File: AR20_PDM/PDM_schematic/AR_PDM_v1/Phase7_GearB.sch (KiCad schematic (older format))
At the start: 15 parts, among them Q1 BTS50025-1TAD, U1 INA233

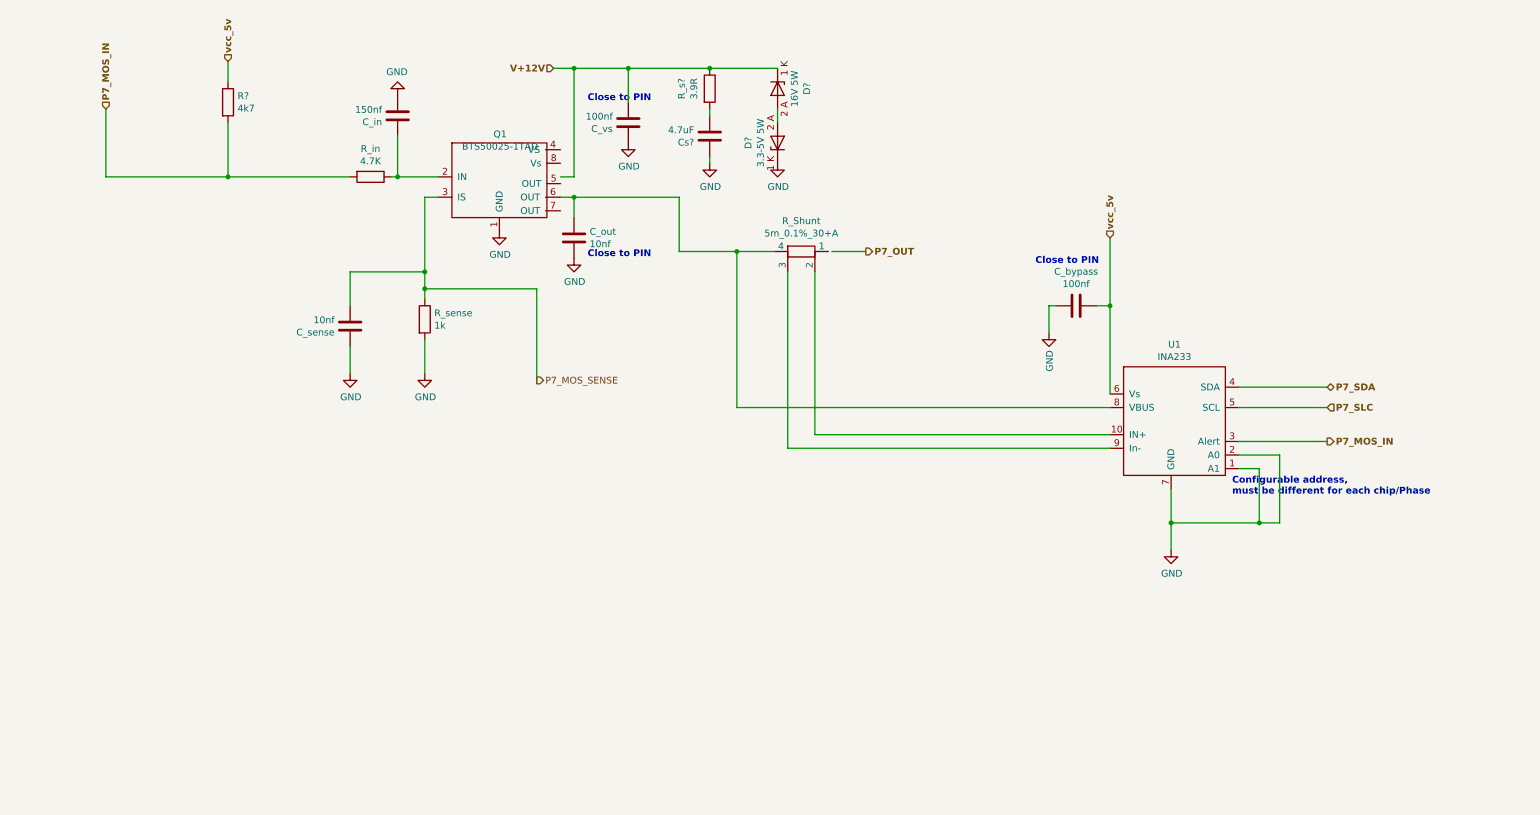
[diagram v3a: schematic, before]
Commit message: Fixed issues, controlled components, BOM, see discription
- added acm symbol
- fixed wrongly faced P-mosfets
- I/O expander now sinks led instead of source
- Bill of material mostly done
- Correct address for INA233 chips.
- Now 4 diodes serves as flyback for all mosfets
- Corrected naming scheme for compmonents (everything is not fixed yet)
- Fixed some labels
- altso some minor changes
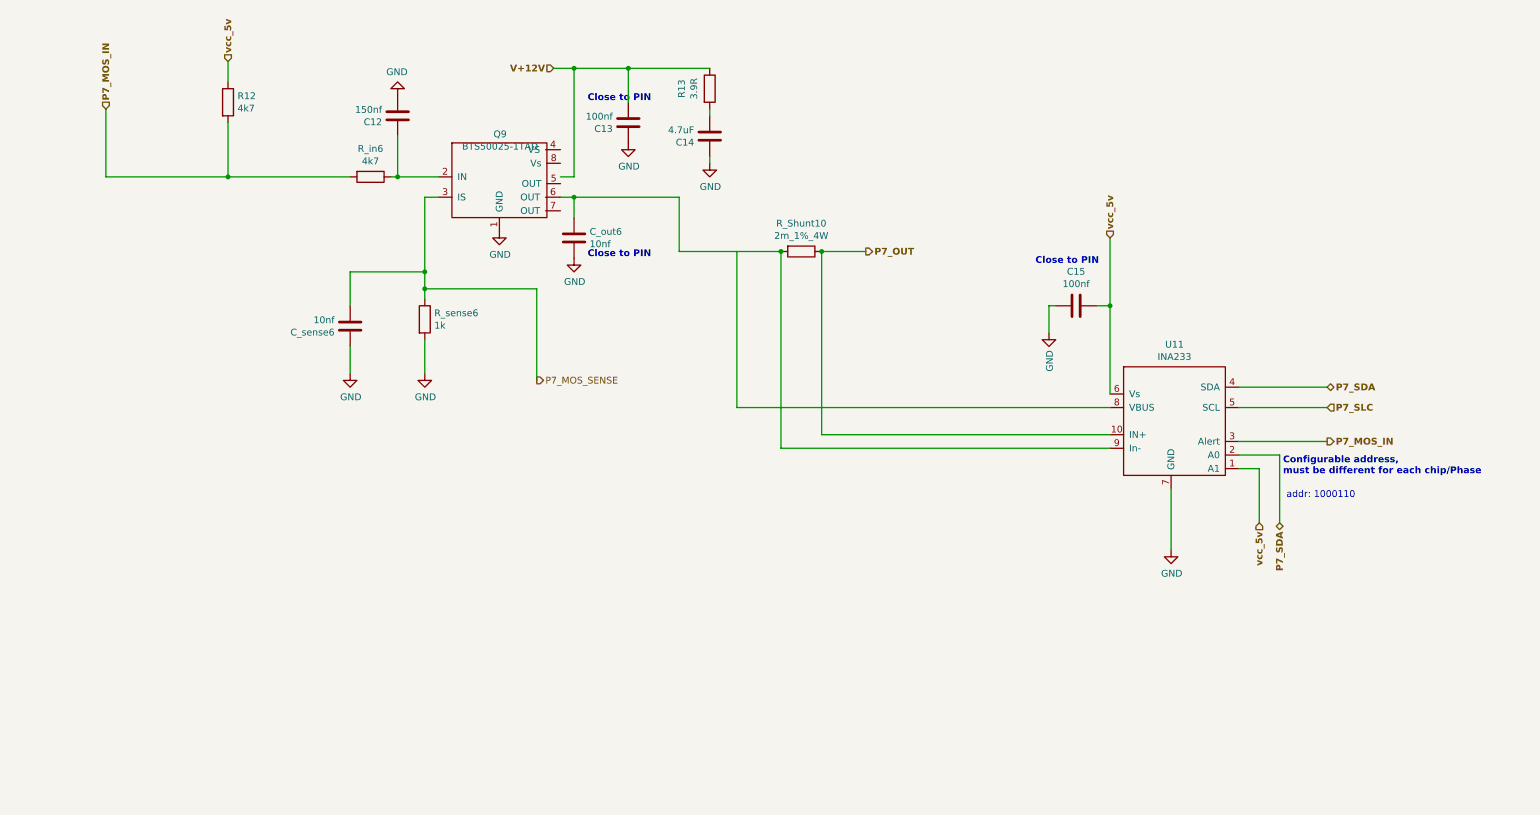
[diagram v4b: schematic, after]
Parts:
- removed C_bypass, C_vs: 100nf, symbol AR20_PDM_v1-rescue:C-Device
- removed C_in: 150nf, symbol AR20_PDM_v1-rescue:C-Device
- removed C_out, C_sense: 10nf, symbol AR20_PDM_v1-rescue:C-Device
- removed Cs?: 4.7uF, symbol AR20_PDM_v1-rescue:C-Device
- removed D?: 3.3-5V 5W, symbol AR20_PDM_v1-rescue:D_Zener-Device
- removed D?: 16V 5W, symbol AR20_PDM_v1-rescue:D_Zener-Device
- removed Q1: BTS50025-1TAD, symbol AR20_PDM_v1-rescue:BTS50025-1TAD
- removed R?: 4k7, symbol AR20_PDM_v1-rescue:R-Device
- removed R_Shunt: 5m_0.1%_30+A, symbol AR20_PDM_v1-rescue:R_Shunt-Device
- removed U1: INA233, symbol AR20_PDM_v1-rescue:INA233
- added C12: 150nf, Capacitor_SMD:C_0603_1608Metric, symbol AR20_PDM_v1-rescue:C-Device
- added C13, C15: 100nf, Capacitor_SMD:C_0603_1608Metric, symbol AR20_PDM_v1-rescue:C-Device
- added C14: 4.7uF, Capacitor_SMD:C_1206_3216Metric, symbol AR20_PDM_v1-rescue:C-Device
- added C_out6, C_sense6: 10nf, Capacitor_SMD:C_0603_1608Metric, symbol AR20_PDM_v1-rescue:C-Device
- added Q9: BTS50025-1TAD, symbol AR20_PDM_v1-rescue:BTS50025-1TAD
- added R12: 4k7, symbol AR20_PDM_v1-rescue:R-Device
- added R_Shunt10: 2m_1%_4W, symbol AR20_PDM_v1-rescue:R-Device
- added U11: INA233, symbol AR20_PDM_v1-rescue:INA233
- R_in6: renamed from R_in; value 4.7K -> 4k7
- gave numbers to parts that had none: 1
- renumbered R_sense to R_sense6
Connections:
- wire segments 57 -> 52
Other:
- note added: "addr: 1000110"

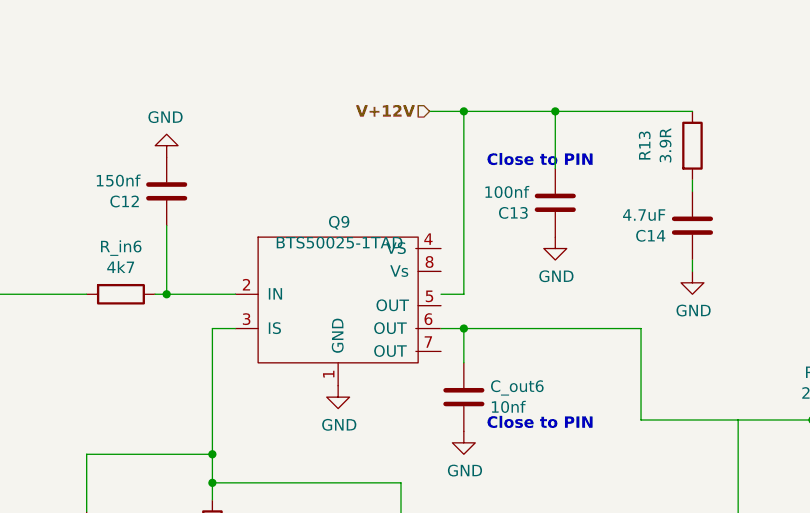
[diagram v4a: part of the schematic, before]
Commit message: PCB design, and issue fixing, work in progress
- Error fixed: Mux mosfet resistor change to ground
- Open drain output added on phase 6, for engine blipping purpose
- Most of pcb symbols and footprints are finished, including main connector
- PCB is change from 1oz to 2oz copper layer, for easier routing.
- Basic Draft of pcb is done, for now.
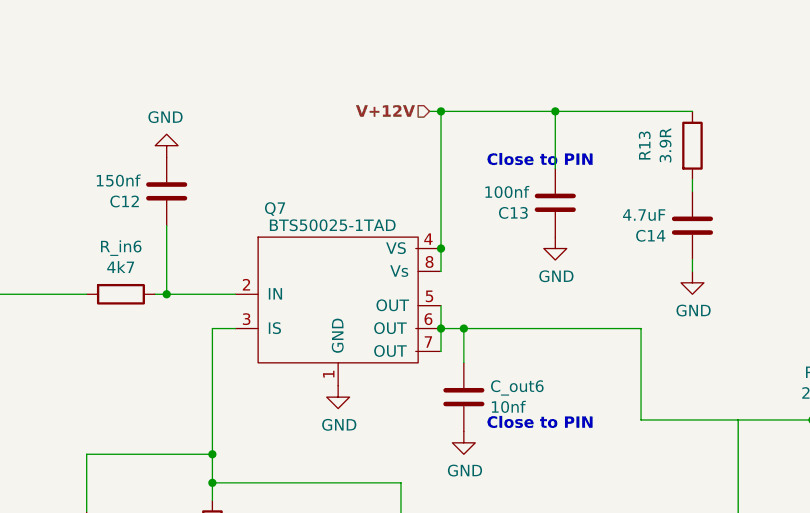
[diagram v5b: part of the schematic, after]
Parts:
- Q7: renamed from Q9; footprint (none) -> AR_PDM_v1:BTS500xx
- R12, R13, R_in6, R_sense6: footprint (none) -> Resistor_SMD:R_0603_1608Metric
- R_Shunt10: footprint (none) -> Resistor_SMD:R_2512_6332Metric
- U11: footprint (none) -> AR_PDM_v1:INA233
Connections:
- net V+12V: now also Q7.4 (VS), Q7.8 (Vs)
- net at C_out6.1, Q7.6 (OUT), R_Shunt10.2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: now also Q7.5 (OUT), Q7.7 (OUT)
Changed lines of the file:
@@
 F 0 "R_in6" V 3093 2400 50  0000 C CNN
 F 1 "4k7" V 3184 2400 50  0000 C CNN
-F 2 "" V 3230 2400 50  0001 C CNN
+F 2 "Resistor_SMD:R_0603_1608Metric" V 3230 2400 50  0001 C CNN
 F 3 "~" H 3300 2400 50  0001 C CNN
 	1    3300 2400
@@
 F 0 "R12" H 2320 1896 50  0000 L CNN
 F 1 "4k7" H 2320 1805 50  0000 L CNN
-F 2 "" V 2180 1850 50  0001 C CNN
+F 2 "Resistor_SMD:R_0603_1608Metric" V 2180 1850 50  0001 C CNN
 F 3 "~" H 2250 1850 50  0001 C CNN
 	1    2250 1850
@@
 $EndComp
 Wire Wire Line
-	4700 2550 4800 2550
-Wire Wire Line
 	4800 2550 4800 2700
 $Comp
@@
 AR Path="/5E0FCFDC/5E21B7FB" Ref="Q?"  Part="1"
 AR Path="/5E0FDCCC/5E21B7FB" Ref="Q?"  Part="1"
-AR Path="/5E10174B/5E21B7FB" Ref="Q9"  Part="1"
-F 0 "Q9" H 4255 3215 50  0000 C CNN
-F 1 "BTS50025-1TAD" H 4255 3124 50  0000 C CNN
-F 2 "" H 4250 2650 50  0001 C CNN
+AR Path="/5E10174B/5E21B7FB" Ref="Q7"  Part="1"
+F 0 "Q7" H 3975 3275 50  0000 C CNN
+F 1 "BTS50025-1TAD" H 4225 3200 50  0000 C CNN
+F 2 "AR_PDM_v1:BTS500xx" H 4250 2650 50  0001 C CNN
 F 3 "" H 4250 2650 50  0001 C CNN
 	1    4250 2650
@@
 F 0 "U11" H 9225 4465 50  0000 C CNN
 F 1 "INA233" H 9225 4374 50  0000 C CNN
-F 2 "" H 9200 4050 50  0001 C CNN
+F 2 "AR_PDM_v1:INA233" H 9200 4050 50  0001 C CNN
 F 3 "" H 9200 4050 50  0001 C CNN
 	1    9200 4050
@@
 Wire Wire Line
 	3700 3100 3700 3225
-Wire Wire Line
-	4700 2400 4800 2400
-Wire Wire Line
-	4800 2400 4800 1600
-Wire Wire Line
-	4800 1600 4650 1600
 Text HLabel 2250 1550 1    50   Input ~ 10
 vcc_5v
@@
 F 0 "R13" V 5593 1750 50  0000 C CNN
 F 1 "3.9R" V 5684 1750 50  0000 C CNN
-F 2 "" V 5730 1750 50  0001 C CNN
+F 2 "Resistor_SMD:R_0603_1608Metric" V 5730 1750 50  0001 C CNN
 F 3 "~" H 5800 1750 50  0001 C CNN
 	1    5800 1750
@@
 Wire Wire Line
 	5200 1600 5800 1600
-Wire Wire Line
-	4800 1600 5200 1600
-Connection ~ 4800 1600
 Connection ~ 5200 1600
 Text HLabel 1350 1900 1    50   Input ~ 10
@@
 F 0 "R_sense6" H 3770 3496 50  0000 L CNN
 F 1 "1k" H 3770 3405 50  0000 L CNN
-F 2 "" V 3630 3450 50  0001 C CNN
+F 2 "Resistor_SMD:R_0603_1608Metric" V 3630 3450 50  0001 C CNN
 F 3 "~" H 3700 3450 50  0001 C CNN
 	1    3700 3450
@@
 F 0 "R_Shunt10" V 6268 2950 50  0000 C CNN
 F 1 "2m_1%_4W" V 6359 2950 50  0000 C CNN
-F 2 "" V 6405 2950 50  0001 C CNN
+F 2 "Resistor_SMD:R_2512_6332Metric" V 6405 2950 50  0001 C CNN
 F 3 "~" H 6475 2950 50  0001 C CNN
 	1    6475 2950
@@
 Text HLabel 10000 4950 3    50   BiDi ~ 10
 P7_SDA
+Wire Wire Line
+	4700 2550 4800 2550
+Wire Wire Line
+	4700 2650 4700 2550
+Connection ~ 4700 2550
+Wire Wire Line
+	4700 2550 4700 2450
+Wire Wire Line
+	4650 1600 4700 1600
+Wire Wire Line
+	4700 2300 4700 2200
+Wire Wire Line
+	4700 2200 4700 1600
+Connection ~ 4700 2200
+Connection ~ 4700 1600
+Wire Wire Line
+	4700 1600 5200 1600
 $EndSCHEMATC

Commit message: PCB Design, Work in progress
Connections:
- net P7_Shunt: now reaches C_out6.1, Q7.5 (OUT), Q7.6 (OUT), Q7.7 (OUT), R_Shunt10.2, U11.8 (VBUS), U11.9 (In-)
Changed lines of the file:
@@
 $Descr A4 11693 8268
 encoding utf-8
-Sheet 10 13
+Sheet 9 13
 Title ""
 Date ""
@@
 Wire Wire Line
 	4700 1600 5200 1600
+Wire Wire Line
+	6000 2950 6000 2825
+Text HLabel 6000 2825 1    50   Input ~ 0
+P7_Shunt
+Connection ~ 6000 2950
 $EndSCHEMATC

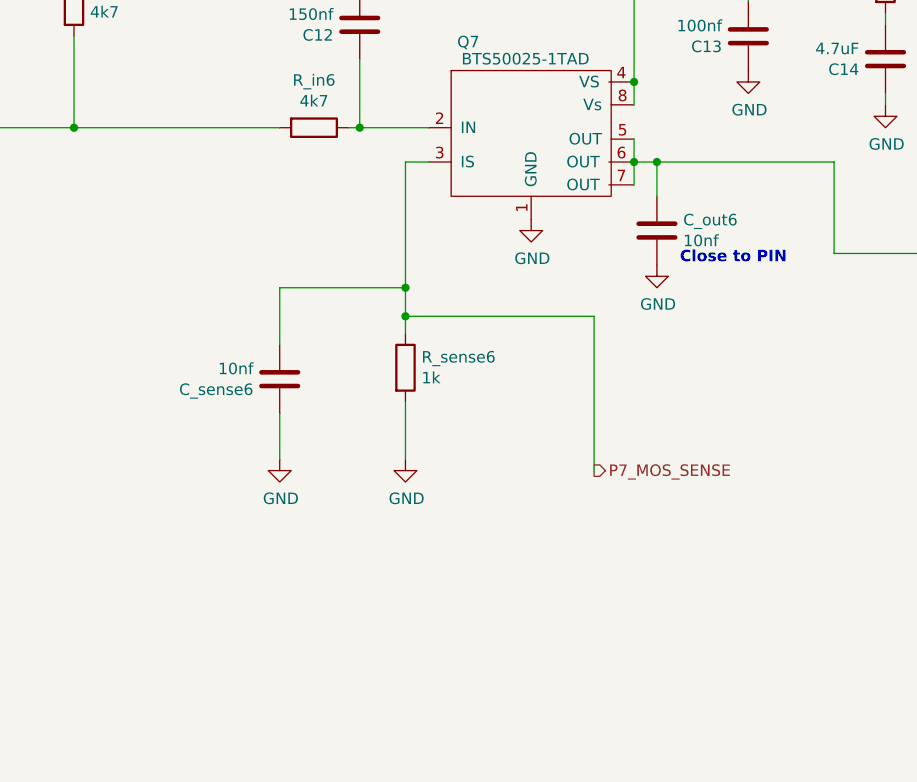
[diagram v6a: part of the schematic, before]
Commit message: PCB Design,  minor schematics changes, work in progress, see description
- Removed mos sense caps and resistors accept one, 
since only one measurement can be done, at a time.
- added mos sens protection resistors on each line, to protect mux mosfets and micro controller. 
- Routing plan mostly finalized, some of the traces are just proof of concept.
those needs to be routed nicely.
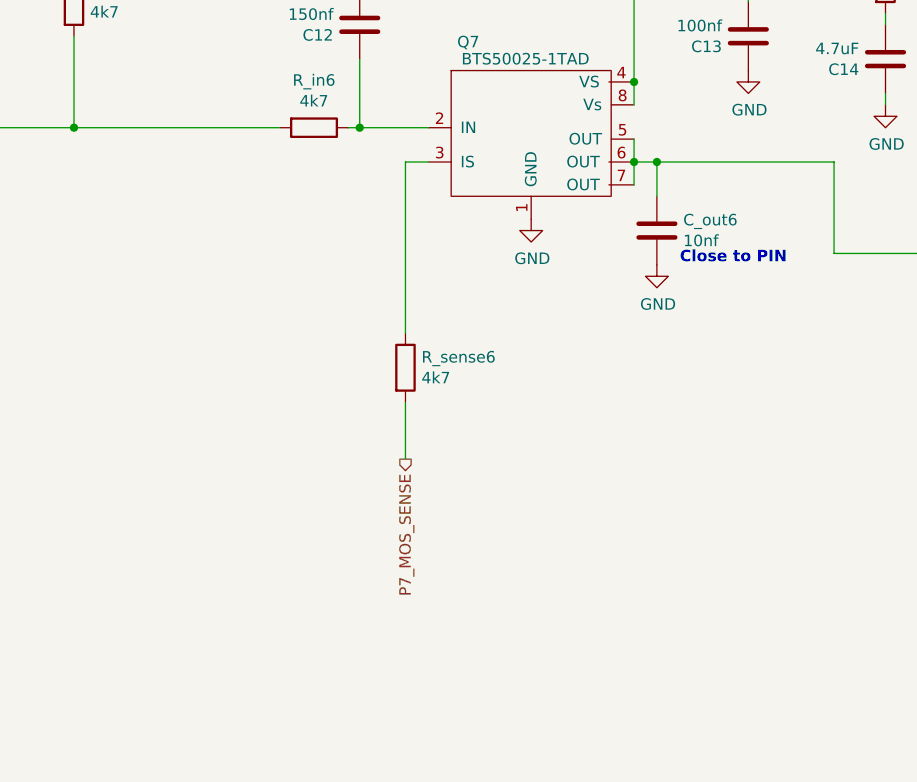
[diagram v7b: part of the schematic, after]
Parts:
- removed C_sense6: 10nf, Capacitor_SMD:C_0603_1608Metric, symbol AR20_PDM_v1-rescue:C-Device
- R_sense6: value 1k -> 4k7
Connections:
- net GND: no longer R_sense6.2
- net P7_MOS_SENSE: now also R_sense6.2; no longer Q7.3 (IS), R_sense6.1
- new net: Q7.3 (IS), R_sense6.1
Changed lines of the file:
@@
-$EndComp
-$Comp
-L AR20_PDM_v1-rescue:GND-power #PWR?
-U 1 1 5E21B820
-P 3700 3850
-AR Path="/5DA89415/5E21B820" Ref="#PWR?"  Part="1"
-AR Path="/5DEB10A1/5E21B820" Ref="#PWR?"  Part="1"
-AR Path="/5DEB20EA/5E21B820" Ref="#PWR?"  Part="1"
-AR Path="/5E0E4725/5E21B820" Ref="#PWR?"  Part="1"
-AR Path="/5E0E4A93/5E21B820" Ref="#PWR?"  Part="1"
-AR Path="/5E0E4EB5/5E21B820" Ref="#PWR?"  Part="1"
-AR Path="/5E0E5304/5E21B820" Ref="#PWR?"  Part="1"
-AR Path="/5E0E594B/5E21B820" Ref="#PWR?"  Part="1"
-AR Path="/5E0E607C/5E21B820" Ref="#PWR?"  Part="1"
-AR Path="/5E0FB5C8/5E21B820" Ref="#PWR?"  Part="1"
-AR Path="/5E0FBBBD/5E21B820" Ref="#PWR?"  Part="1"
-AR Path="/5E0FC3A2/5E21B820" Ref="#PWR?"  Part="1"
-AR Path="/5E0FCFDC/5E21B820" Ref="#PWR?"  Part="1"
-AR Path="/5E0FDCCC/5E21B820" Ref="#PWR?"  Part="1"
-AR Path="/5E10174B/5E21B820" Ref="#PWR083"  Part="1"
-F 0 "#PWR083" H 3700 3600 50  0001 C CNN
-F 1 "GND" H 3705 3677 50  0000 C CNN
-F 2 "" H 3700 3850 50  0001 C CNN
-F 3 "" H 3700 3850 50  0001 C CNN
-	1    3700 3850
-	1    0    0    -1
 $EndComp
 $Comp
@@
 $EndComp
 Wire Wire Line
-	3700 2550 3700 3100
-Wire Wire Line
 	3700 2550 3800 2550
 Wire Wire Line
@@
 Wire Wire Line
 	9700 4450 10000 4450
-$Comp
-L AR20_PDM_v1-rescue:GND-power #PWR?
-U 1 1 5E21B84C
-P 3150 3850
-AR Path="/5DA89415/5E21B84C" Ref="#PWR?"  Part="1"
-AR Path="/5DEB10A1/5E21B84C" Ref="#PWR?"  Part="1"
-AR Path="/5DEB20EA/5E21B84C" Ref="#PWR?"  Part="1"
-AR Path="/5E0E4725/5E21B84C" Ref="#PWR?"  Part="1"
-AR Path="/5E0E4A93/5E21B84C" Ref="#PWR?"  Part="1"
-AR Path="/5E0E4EB5/5E21B84C" Ref="#PWR?"  Part="1"
-AR Path="/5E0E5304/5E21B84C" Ref="#PWR?"  Part="1"
-AR Path="/5E0E594B/5E21B84C" Ref="#PWR?"  Part="1"
-AR Path="/5E0E607C/5E21B84C" Ref="#PWR?"  Part="1"
-AR Path="/5E0FB5C8/5E21B84C" Ref="#PWR?"  Part="1"
-AR Path="/5E0FBBBD/5E21B84C" Ref="#PWR?"  Part="1"
-AR Path="/5E0FC3A2/5E21B84C" Ref="#PWR?"  Part="1"
-AR Path="/5E0FCFDC/5E21B84C" Ref="#PWR?"  Part="1"
-AR Path="/5E0FDCCC/5E21B84C" Ref="#PWR?"  Part="1"
-AR Path="/5E10174B/5E21B84C" Ref="#PWR081"  Part="1"
-F 0 "#PWR081" H 3150 3600 50  0001 C CNN
-F 1 "GND" H 3155 3677 50  0000 C CNN
-F 2 "" H 3150 3850 50  0001 C CNN
-F 3 "" H 3150 3850 50  0001 C CNN
-	1    3150 3850
-	1    0    0    -1
-$EndComp
-$Comp
-L AR20_PDM_v1-rescue:C-Device C_sense?
-U 1 1 5E21B84F
-P 3150 3500
-AR Path="/5DA89415/5E21B84F" Ref="C_sense?"  Part="1"
-AR Path="/5DEB10A1/5E21B84F" Ref="C_sense?"  Part="1"
-AR Path="/5DEB20EA/5E21B84F" Ref="C_sense?"  Part="1"
-AR Path="/5E0E4725/5E21B84F" Ref="C_sense?"  Part="1"
-AR Path="/5E0E4A93/5E21B84F" Ref="C_sense?"  Part="1"
-AR Path="/5E0E4EB5/5E21B84F" Ref="C_sense?"  Part="1"
-AR Path="/5E0E5304/5E21B84F" Ref="C_sense?"  Part="1"
-AR Path="/5E0E594B/5E21B84F" Ref="C_sense?"  Part="1"
-AR Path="/5E0E607C/5E21B84F" Ref="C_sense?"  Part="1"
-AR Path="/5E0FB5C8/5E21B84F" Ref="C_sense?"  Part="1"
-AR Path="/5E0FBBBD/5E21B84F" Ref="C_sense?"  Part="1"
-AR Path="/5E0FC3A2/5E21B84F" Ref="C_sense?"  Part="1"
-AR Path="/5E0FCFDC/5E21B84F" Ref="C_sense?"  Part="1"
-AR Path="/5E0FDCCC/5E21B84F" Ref="C_sense?"  Part="1"
-AR Path="/5E10174B/5E21B84F" Ref="C_sense6"  Part="1"
-F 0 "C_sense6" H 3265 3546 50  0000 L CNN
-F 1 "10nf" H 3265 3455 50  0000 L CNN
-F 2 "Capacitor_SMD:C_0603_1608Metric" H 3188 3350 50  0001 C CNN
-F 3 "~" H 3150 3500 50  0001 C CNN
-	1    3150 3500
-	-1   0    0    1
-$EndComp
 Wire Wire Line
 	3450 2400 3500 2400
@@
 Text Notes 8200 3050 0    50   ~ 10
 Close to PIN
-Wire Wire Line
-	3150 3100 3150 3350
-Wire Wire Line
-	3150 3650 3150 3850
-Wire Wire Line
-	3150 3100 3700 3100
-Connection ~ 3700 3100
-Wire Wire Line
-	3700 3100 3700 3225
 Text HLabel 2250 1550 1    50   Input ~ 10
 vcc_5v
@@
 Wire Wire Line
 	6000 4100 8750 4100
-$Comp
-L AR20_PDM_v1-rescue:R-Device R_sense?
-U 1 1 5E0E437E
-P 3700 3450
-AR Path="/5DA89415/5E0E437E" Ref="R_sense?"  Part="1"
-AR Path="/5DEB10A1/5E0E437E" Ref="R_sense?"  Part="1"
-AR Path="/5DEB20EA/5E0E437E" Ref="R_sense?"  Part="1"
-AR Path="/5E0E4725/5E0E437E" Ref="R_sense?"  Part="1"
-AR Path="/5E0E4A93/5E0E437E" Ref="R_sense?"  Part="1"
-AR Path="/5E0E4EB5/5E0E437E" Ref="R_sense?"  Part="1"
-AR Path="/5E0E5304/5E0E437E" Ref="R_sense?"  Part="1"
-AR Path="/5E0E594B/5E0E437E" Ref="R_sense?"  Part="1"
-AR Path="/5E0E607C/5E0E437E" Ref="R_sense?"  Part="1"
-AR Path="/5E0FB5C8/5E0E437E" Ref="R_sense?"  Part="1"
-AR Path="/5E0FBBBD/5E0E437E" Ref="R_sense?"  Part="1"
-AR Path="/5E0FC3A2/5E0E437E" Ref="R_sense?"  Part="1"
-AR Path="/5E0FCFDC/5E0E437E" Ref="R_sense?"  Part="1"
-AR Path="/5E0FDCCC/5E0E437E" Ref="R_sense?"  Part="1"
-AR Path="/5E10174B/5E0E437E" Ref="R_sense6"  Part="1"
-F 0 "R_sense6" H 3770 3496 50  0000 L CNN
-F 1 "1k" H 3770 3405 50  0000 L CNN
-F 2 "Resistor_SMD:R_0603_1608Metric" V 3630 3450 50  0001 C CNN
-F 3 "~" H 3700 3450 50  0001 C CNN
-	1    3700 3450
-	1    0    0    -1
-$EndComp
 Wire Wire Line
 	6625 4300 8750 4300
-Wire Wire Line
-	3700 3225 4525 3225
-Wire Wire Line
-	4525 3225 4525 3900
-Connection ~ 3700 3225
-Wire Wire Line
-	3700 3225 3700 3300
-Text HLabel 4525 3900 2    50   Output ~ 0
-P7_MOS_SENSE
 Wire Wire Line
 	6000 4100 6000 2950
@@
 P7_Shunt
 Connection ~ 6000 2950
+Wire Wire Line
+	3700 2550 3700 3300
+$Comp
+L AR20_PDM_v1-rescue:R-Device R_sense?
+U 1 1 5E0E437E
+P 3700 3450
+AR Path="/5DA89415/5E0E437E" Ref="R_sense?"  Part="1"
+AR Path="/5DEB10A1/5E0E437E" Ref="R_sense?"  Part="1"
+AR Path="/5DEB20EA/5E0E437E" Ref="R_sense?"  Part="1"
+AR Path="/5E0E4725/5E0E437E" Ref="R_sense?"  Part="1"
+AR Path="/5E0E4A93/5E0E437E" Ref="R_sense?"  Part="1"
+AR Path="/5E0E4EB5/5E0E437E" Ref="R_sense?"  Part="1"
+AR Path="/5E0E5304/5E0E437E" Ref="R_sense?"  Part="1"
+AR Path="/5E0E594B/5E0E437E" Ref="R_sense?"  Part="1"
+AR Path="/5E0E607C/5E0E437E" Ref="R_sense?"  Part="1"
+AR Path="/5E0FB5C8/5E0E437E" Ref="R_sense?"  Part="1"
+AR Path="/5E0FBBBD/5E0E437E" Ref="R_sense?"  Part="1"
+AR Path="/5E0FC3A2/5E0E437E" Ref="R_sense?"  Part="1"
+AR Path="/5E0FCFDC/5E0E437E" Ref="R_sense?"  Part="1"
+AR Path="/5E0FDCCC/5E0E437E" Ref="R_sense?"  Part="1"
+AR Path="/5E10174B/5E0E437E" Ref="R_sense6"  Part="1"
+F 0 "R_sense6" H 3770 3496 50  0000 L CNN
+F 1 "4k7" H 3770 3405 50  0000 L CNN
+F 2 "Resistor_SMD:R_0603_1608Metric" V 3630 3450 50  0001 C CNN
+F 3 "~" H 3700 3450 50  0001 C CNN
+	1    3700 3450
+	1    0    0    -1
+$EndComp
+Text HLabel 3700 3850 3    50   Output ~ 0
+P7_MOS_SENSE
 $EndSCHEMATC
